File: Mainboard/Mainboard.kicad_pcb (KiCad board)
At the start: 2 copper layers, 46 parts, among them IC1 REF102AU_2K5, IC4 DAC8814IBDBT, J1 5745782-6, J2 5745782-6, J3 5745782-6, U1 Teensy4.0, U11 ADG419BR, U12 ADG419BR, U7 ADG419BR, U8 LTC2326CMS-16-PBF, U9 LT1469CS8-TRPBF

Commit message: working mainboard push!
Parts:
- removed C121: 330u 25V, Capacitor_THT:CP_Radial_D8.0mm_P3.50mm
- removed C126, C127, C128, C129, C133, C135, C136, C137: 10u, Capacitor_SMD:C_1206_3216Metric
- removed TP1, TP2, TP3, TP4, TP5, TP6, TP7, TP8: TestPoint, TestPoint:TestPoint_Loop_D1.80mm_Drill1.0mm_Beaded
- added A1: Pololu_Breakout_A4988, Module:Pololu_Breakout-16_15.2x20.3mm, F.Cu at (179.3, 120.8)
- added A2: Pololu_Breakout_A4988, Module:Pololu_Breakout-16_15.2x20.3mm, F.Cu at (158.6, 111.1)
- added A3: Pololu_Breakout_A4988, Module:Pololu_Breakout-16_15.2x20.3mm, F.Cu at (158.6, 133.9)
- added C10: 4.7n, Capacitor_SMD:C_0805_2012Metric, F.Cu at (138.6, 95.2)
- added C11: 4.7n, Capacitor_SMD:C_0805_2012Metric, F.Cu at (140.1, 82.8)
- added C12: 4.7n, Capacitor_SMD:C_0805_2012Metric, F.Cu at (144.6, 87.8)
- added C13: 4.7n, Capacitor_SMD:C_0805_2012Metric, F.Cu at (144.6, 63.2)
- added C14: 4.7n, Capacitor_SMD:C_0805_2012Metric, F.Cu at (138.6, 70.8)
- added C15: 4.7n, Capacitor_SMD:C_0805_2012Metric, F.Cu at (140.1, 58.8)
- added C16: 3.3n, Capacitor_SMD:C_0805_2012Metric, F.Cu at (164.5, 78.4)
- added C17: 100n, Capacitor_SMD:C_0805_2012Metric, F.Cu at (135.1, 63.8)
- added C18: 100n, Capacitor_SMD:C_0805_2012Metric, F.Cu at (145.1, 67.8)
- added C19: 100n, Capacitor_SMD:C_0805_2012Metric, F.Cu at (145.1, 92.2)
- added C20: 100n, Capacitor_SMD:C_0805_2012Metric, F.Cu at (135.1, 86.3)
- added C21: 3.3n, Capacitor_SMD:C_0805_2012Metric, F.Cu at (179.0, 70.3)
- added C22: 3.3n, Capacitor_SMD:C_0805_2012Metric, F.Cu at (179.0, 78.3)
- added C23: 3.3n, Capacitor_SMD:C_0805_2012Metric, F.Cu at (164.5, 70.4)
- added C24: 4.7n, Capacitor_SMD:C_0805_2012Metric, F.Cu at (157.2, 80.3)
- added C25: 4.7n, Capacitor_SMD:C_0805_2012Metric, F.Cu at (171.6, 67.3)
- added C26: 4.7n, Capacitor_SMD:C_0805_2012Metric, F.Cu at (171.6, 80.3)
- added C27: 4.7n, Capacitor_SMD:C_0805_2012Metric, F.Cu at (157.2, 67.3)
- added C28: 100n, Capacitor_SMD:C_0805_2012Metric, F.Cu at (175.6, 119.8)
- added C29: 3.3n, Capacitor_SMD:C_0805_2012Metric, F.Cu at (173.4, 94.4)
- added C30: 3.3n, Capacitor_SMD:C_0805_2012Metric, F.Cu at (180.2, 103.5)
- added C31: 3.3n, Capacitor_SMD:C_0805_2012Metric, F.Cu at (173.6, 104.7)
- added C32: 3.3n, Capacitor_SMD:C_0805_2012Metric, F.Cu at (185.3, 103.5)
- added C33: 47u, Capacitor_SMD:C_0805_2012Metric, F.Cu at (192.3, 93.7)
- added C34: 100n, Capacitor_SMD:C_0805_2012Metric, F.Cu at (188.6, 93.7)
- added C35: 10u, Capacitor_THT:CP_Radial_D5.0mm_P2.00mm, F.Cu at (181.6, 88.9)
- added C36: 100n, Capacitor_SMD:C_0805_2012Metric, F.Cu at (182.6, 93.2)
- added C37: 100n, Capacitor_SMD:C_0805_2012Metric, F.Cu at (175.6, 142.8)
- added C38: 100n, Capacitor_SMD:C_0805_2012Metric, F.Cu at (196.3, 129.6)
- added C39: 100n, Capacitor_SMD:C_0805_2012Metric, F.Cu at (209.7, 78.1)
- added C40: 100n, Capacitor_SMD:C_0805_2012Metric, F.Cu at (167.9, 74.4)
- added C41: 100n, Capacitor_SMD:C_0805_2012Metric, F.Cu at (179.0, 74.3)
- added C42: 100n, Capacitor_SMD:C_0805_2012Metric, F.Cu at (153.4, 74.4)
- added C43: 100n, Capacitor_SMD:C_0805_2012Metric, F.Cu at (164.5, 74.4)
- added C44: 100n, Capacitor_SMD:C_0805_2012Metric, F.Cu at (195.6, 60.8)
- added C45: 100n, Capacitor_SMD:C_0805_2012Metric, F.Cu at (192.1, 50.0)
- added C46: 100n, Capacitor_SMD:C_0805_2012Metric, F.Cu at (164.5, 58.0)
- added C47: 100n, Capacitor_SMD:C_0805_2012Metric, F.Cu at (153.8, 61.2)
- added C79: 100u, Capacitor_THT:CP_Radial_D6.3mm_P2.50mm, F.Cu at (152.6, 128.9)
- added C8: 2.2u, Capacitor_SMD:C_0805_2012Metric, F.Cu at (187.4, 50.0)
- added C80: 100u, Capacitor_THT:CP_Radial_D6.3mm_P2.50mm, F.Cu at (184.6, 144.4)
- added C83: 100u, Capacitor_THT:CP_Radial_D6.3mm_P2.50mm, F.Cu at (152.6, 151.8)
- added C84: 10u, Capacitor_THT:CP_Radial_D5.0mm_P2.00mm, F.Cu at (182.1, 56.8)
- added C85: 100u, Capacitor_THT:CP_Radial_D6.3mm_P2.50mm, F.Cu at (182.1, 47.9)
- added H1: MountingHole_Pad, MountingHole:MountingHole_2.2mm_M2_Pad_Via, F.Cu at (220.3, 154.8)
- added J4: Conn_01x02_Pin, Connector_PinHeader_2.54mm:PinHeader_1x02_P2.54mm_Vertical, F.Cu at (158.3, 88.1)
- added J5: Conn_01x02_Pin, Connector_PinHeader_2.54mm:PinHeader_1x02_P2.54mm_Vertical, F.Cu at (189.8, 100.3)
- added R19: 1k, Resistor_SMD:R_0805_2012Metric, F.Cu at (191.1, 47.5)
- added R20: 3k, Resistor_SMD:R_0805_2012Metric, F.Cu at (138.6, 98.8)
- added R21: 220, Resistor_SMD:R_0805_2012Metric, F.Cu at (135.1, 94.2)
- added R22: 3k, Resistor_SMD:R_0805_2012Metric, F.Cu at (145.2, 95.3)
- added R23: 3k, Resistor_SMD:R_0805_2012Metric, F.Cu at (145.2, 98.7)
- added R24: 220, Resistor_SMD:R_0805_2012Metric, F.Cu at (135.1, 81.8)
- added R25: 3k, Resistor_SMD:R_0805_2012Metric, F.Cu at (140.1, 79.2)
- added R26: 3k, Resistor_SMD:R_0805_2012Metric, F.Cu at (146.8, 84.1)
- added R27: 3k, Resistor_SMD:R_0805_2012Metric, F.Cu at (148.1, 87.8)
- added R28: 3k, Resistor_SMD:R_0805_2012Metric, F.Cu at (145.0, 79.2)
- added R29: 3k, Resistor_SMD:R_0805_2012Metric, F.Cu at (145.0, 74.3)
- added R30: 1M2, Resistor_SMD:R_0805_2012Metric, F.Cu at (209.8, 81.9)
- added R31: 3k, Resistor_SMD:R_0805_2012Metric, F.Cu at (145.1, 70.8)
- added R32: 3k, Resistor_SMD:R_0805_2012Metric, F.Cu at (144.6, 55.8)
- added R33: 3k, Resistor_SMD:R_0805_2012Metric, F.Cu at (146.6, 59.8)
- added R34: 3k, Resistor_SMD:R_0805_2012Metric, F.Cu at (147.6, 63.2)
- added R35: 3k, Resistor_SMD:R_0805_2012Metric, F.Cu at (138.6, 74.2)
- added R36: 3k, Resistor_SMD:R_0805_2012Metric, F.Cu at (140.1, 55.8)
- added R37: 220, Resistor_SMD:R_0805_2012Metric, F.Cu at (135.1, 73.2)
- added R38: 220, Resistor_SMD:R_0805_2012Metric, F.Cu at (135.1, 59.3)
- added R39: 10k, Resistor_SMD:R_0805_2012Metric, F.Cu at (188.5, 67.8)
- added R40: 1.5k, Resistor_SMD:R_0805_2012Metric, F.Cu at (161.2, 64.4)
- added R41: 1.5k, Resistor_SMD:R_0805_2012Metric, F.Cu at (175.6, 80.3)
- added R42: 1.5k, Resistor_SMD:R_0805_2012Metric, F.Cu at (175.5, 64.3)
- added R43: 1.5k, Resistor_SMD:R_0805_2012Metric, F.Cu at (161.2, 80.3)
- added R50: 3k, Resistor_SMD:R_0805_2012Metric, F.Cu at (161.2, 83.1)
- added R51: 3k, Resistor_SMD:R_0805_2012Metric, F.Cu at (157.2, 83.1)
- added R52: 3k, Resistor_SMD:R_0805_2012Metric, F.Cu at (175.5, 67.3)
- added R53: 3k, Resistor_SMD:R_0805_2012Metric, F.Cu at (171.5, 64.3)
- added R54: 3k, Resistor_SMD:R_0805_2012Metric, F.Cu at (175.5, 83.3)
- added R55: 3k, Resistor_SMD:R_0805_2012Metric, F.Cu at (171.5, 83.3)
- added R56: 3k, Resistor_SMD:R_0805_2012Metric, F.Cu at (161.2, 67.3)
- added R57: 3k, Resistor_SMD:R_0805_2012Metric, F.Cu at (157.2, 64.4)
- added R58: 3k, Resistor_SMD:R_0805_2012Metric, F.Cu at (164.5, 62.2)
- added R59: 470, Resistor_SMD:R_0805_2012Metric, F.Cu at (164.5, 88.8)
- added R60: 100, Resistor_SMD:R_0805_2012Metric, F.Cu at (195.9, 88.2)
- added R61: 470, Resistor_SMD:R_0805_2012Metric, F.Cu at (169.3, 94.4)
- added R62: 470, Resistor_SMD:R_0805_2012Metric, F.Cu at (164.5, 99.0)
- added R63: 470, Resistor_SMD:R_0805_2012Metric, F.Cu at (169.3, 104.7)
- added R64: 10k, Resistor_SMD:R_0805_2012Metric, F.Cu at (195.9, 90.4)
- added U10: TL072, Package_SO:SOIC-8-1EP_3.9x4.9mm_P1.27mm_EP2.29x3mm_ThermalVias, F.Cu at (157.0, 93.4)
- added U2: TL072, Package_SO:SOIC-8-1EP_3.9x4.9mm_P1.27mm_EP2.29x3mm_ThermalVias, F.Cu at (194.6, 55.5)
- added U3: TL072, Package_SO:SOIC-8-1EP_3.9x4.9mm_P1.27mm_EP2.29x3mm_ThermalVias, F.Cu at (139.6, 89.4)
- added U4: TL072, Package_SO:SOIC-8-1EP_3.9x4.9mm_P1.27mm_EP2.29x3mm_ThermalVias, F.Cu at (139.6, 65.1)
- added U5: TL074, Package_SO:SOIC-14_3.9x8.7mm_P1.27mm, F.Cu at (159.0, 73.8)
- added U6: TL074, Package_SO:SOIC-14_3.9x8.7mm_P1.27mm, F.Cu at (173.5, 73.7)
- C122, C123, C124, C125, C130, C131, C132, C134: value 10u -> 100n; footprint Capacitor_SMD:C_1206_3216Metric -> Capacitor_SMD:C_0805_2012Metric
- C77, C78, C81, C82: value 330u 25V -> 10u; footprint Capacitor_THT:CP_Radial_D8.0mm_P3.50mm -> Capacitor_THT:CP_Radial_D5.0mm_P2.00mm
- moved JP12 102.8 mm to (214.3, 81.9), turned to 180 degrees
- moved JP29 100.7 mm to (214.2, 78.1), turned to 180 degrees
- moved J1 89.0 mm to (214.2, 45.5), turned to 90 degrees
- moved JP32 76.1 mm to (194.1, 97.5)
- moved JP33 75.9 mm to (194.1, 100.7)
- moved U1 74.0 mm to (138.2, 43.9)
- moved IC1 71.5 mm to (188.4, 55.5), turned to 90 degrees
- moved U12 70.8 mm to (174.1, 100.2)
- moved JP31 69.9 mm to (168.0, 99.0), turned to 90 degrees
- moved C82 67.7 mm to (204.0, 62.5), turned to -90 degrees
- moved U11 67.6 mm to (174.1, 90.0)
- moved C81 66.6 mm to (204.0, 55.5), turned to -90 degrees
- moved U8 66.0 mm to (189.4, 89.9)
- moved C78 65.5 mm to (204.0, 48.5), turned to -90 degrees
- moved C77 64.0 mm to (204.0, 43.5), turned to 90 degrees
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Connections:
- net /ADC/AIN+ renamed /AIN+
- net /ADC/AIN- renamed /AIN-
- net /DAC/BIAS_MOD renamed /BIAS_MOD
- net /DAC/CS_DAC renamed /CS_DAC
- net /DAC/MOSI_DAC renamed /MOSI_DAC
- C130 pad 1: -15V -> +3V3
- C131 pad 2: +15V -> +5V
- C132 pad 1: -15V -> GND
- C132 pad 2: GND -> +5V
- C134 pad 1: -15V -> +3V3
- IC4 pad 21: /DAC/LDAC_DAC -> /LDAC_DAC
- IC4 pad 9: /DAC/SCK_DAC -> /SCK_ADC
- J1 pad MH1: /Shield -> Shield
- J1 pad MH2: /Shield -> Shield
- J2 pad 1: /Connectors/T_Amp+ -> /T_Amp-
- J2 pad 14: GND -> unconnected-(J2-Pad14)
- J2 pad 15: GND -> /Z-Y
- J2 pad 2: /Connectors/T_Amp- -> /T_Amp+
- J2 pad 3: unconnected-(J2-Pad3) -> GND
- J2 pad 4: unconnected-(J2-Pad4) -> /Z+X
- J2 pad 5: unconnected-(J2-Pad5) -> /Z-X
- J2 pad 7: unconnected-(J2-Pad7) -> /Connectors/BIAS
- J2 pad 8: unconnected-(J2-Pad8) -> /Z+Y
- J2 pad MH1: GND -> Shield
- J2 pad MH2: GND -> Shield
- J3 pad 1: unconnected-(J3-Pad1) -> /2B_3
- J3 pad 10: unconnected-(J3-Pad10) -> -15V
- J3 pad 11: unconnected-(J3-Pad11) -> GND
- J3 pad 12: unconnected-(J3-Pad12) -> /2B_2
- J3 pad 13: unconnected-(J3-Pad13) -> /1A_2
- J3 pad 14: unconnected-(J3-Pad14) -> /2B_1
- J3 pad 15: unconnected-(J3-Pad15) -> /1B_1
- J3 pad 2: unconnected-(J3-Pad2) -> /2A_3
- J3 pad 3: unconnected-(J3-Pad3) -> /1A_3
- J3 pad 4: unconnected-(J3-Pad4) -> /1B_3
- J3 pad 5: unconnected-(J3-Pad5) -> /2A_2
- J3 pad 6: unconnected-(J3-Pad6) -> /1B_2
- J3 pad 7: unconnected-(J3-Pad7) -> /2A_1
- J3 pad 8: unconnected-(J3-Pad8) -> /1A_1
- J3 pad 9: unconnected-(J3-Pad9) -> +15V
- J3 pad MH1: GND -> Shield
- J3 pad MH2: GND -> Shield
- JP12 pad 1: /Shield -> Shield
- JP29 pad 1: /Shield -> Shield
- JP30 pad 1: /ADC/T_Amp+ -> /T_Amp+
- JP31 pad 1: /ADC/T_Amp- -> /T_Amp-
- U1 pad 11: /DAC/LDAC_DAC -> /CS_ADC
- U1 pad 14: unconnected-(U1-12_MISO_MQSL-Pad14) -> /MISO_ADC
- U1 pad 17: GND -> unconnected-(U1-GND-Pad17)
- U1 pad 2: unconnected-(U1-0_RX1_CRX2_CS1-Pad2) -> /BIAS_MOD_EN
- U1 pad 20: /DAC/SCK_DAC -> /SCK_ADC
- U1 pad 21: unconnected-(U1-14_A0_TX3_SPDIF_OUT-Pad21) -> /StepperDrivers/DIR_1
- U1 pad 22: unconnected-(U1-15_A1_RX3_SPDIF_IN-Pad22) -> /StepperDrivers/STEP_1
- U1 pad 3: unconnected-(U1-1_TX1_CTX2_MISO1-Pad3) -> /StepperDrivers/STEP_3
- U1 pad 32: GND -> unconnected-(U1-GND-Pad32)
- U1 pad 4: unconnected-(U1-2_OUT2-Pad4) -> /StepperDrivers/DIR_3
- U1 pad 5: unconnected-(U1-3_LRCLK2-Pad5) -> /StepperDrivers/STEP_2
- U1 pad 6: unconnected-(U1-4_BCLK2-Pad6) -> /StepperDrivers/DIR_2
- U1 pad 7: unconnected-(U1-5_IN2-Pad7) -> /BUSY_ADC
- U1 pad 8: unconnected-(U1-6_OUT1D-Pad8) -> /CNV_ADC
- U1 pad 9: unconnected-(U1-7_RX2_OUT1A-Pad9) -> /LDAC_DAC
- U11 pad 2: /ADC/T_Amp+ -> /T_Amp+
- U12 pad 2: /ADC/T_Amp- -> /T_Amp-
- U7 pad 6: /DAC/BIAS_MOD_EN -> /BIAS_MOD_EN
- U8 pad 11: /ADC/BUSY_ADC -> /BUSY_ADC
- U8 pad 12: /ADC/~CS_ADC -> /CS_ADC
- U8 pad 13: /ADC/SCK_ADC -> /SCK_ADC
- U8 pad 9: /ADC/CNV -> /CNV_ADC
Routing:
- net +5V: track 0.00 -> 215.9 mm, vias 0 -> 6
- net GND: track 0.00 -> 161.3 mm, vias 0 -> 56
- net /StepperDrivers/STEP_1: track 0.00 -> 135.6 mm, vias 0 -> 3
- net /StepperDrivers/DIR_1: track 0.00 -> 130.1 mm, vias 0 -> 2
- net /StepperDrivers/STEP_3: track 0.00 -> 120.6 mm, vias 0 -> 2
- net /StepperDrivers/DIR_3: track 0.00 -> 119.3 mm, vias 0 -> 3
- net /StepperDrivers/STEP_2: track 0.00 -> 107.7 mm
- net /PS_Temp_SCL: track 0.00 -> 107.0 mm, vias 0 -> 2
- net /StepperDrivers/DIR_2: track 0.00 -> 105.6 mm
- net -15V: track 0.00 -> 102.2 mm, vias 0 -> 10
- net +15V: track 0.00 -> 101.2 mm, vias 0 -> 10
- net /PS_Temp_SDA: track 0.00 -> 92.5 mm
- net /CNV_ADC: track 0.00 -> 85.8 mm, vias 0 -> 3
- net +3V3: track 0.00 -> 84.9 mm, vias 0 -> 4
- net /BUSY_ADC: track 0.00 -> 84.8 mm, vias 0 -> 2
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- added copper zone on In1.Cu, net +15V
- added copper zone on In1.Cu, net +3V3
- added copper zone on In2.Cu, net +5V
- added copper zone on In2.Cu, net -15V
- added copper zone on B.Cu, net GND
- added copper zone on F.Cu, net Shield
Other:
- board outline added: 106.1 x 132 mm
- copper layers 2 -> 4

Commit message: more push
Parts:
- added G***: LOGO, LOGO, F.Cu at (210.0, 126.8)
- added G***: LOGO, LOGO, F.Cu at (189.6, 110.9)
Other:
- board text added: "STM Mainboard Author: Gautham Anne 4/02/2025"
- board text added: "V1.1"

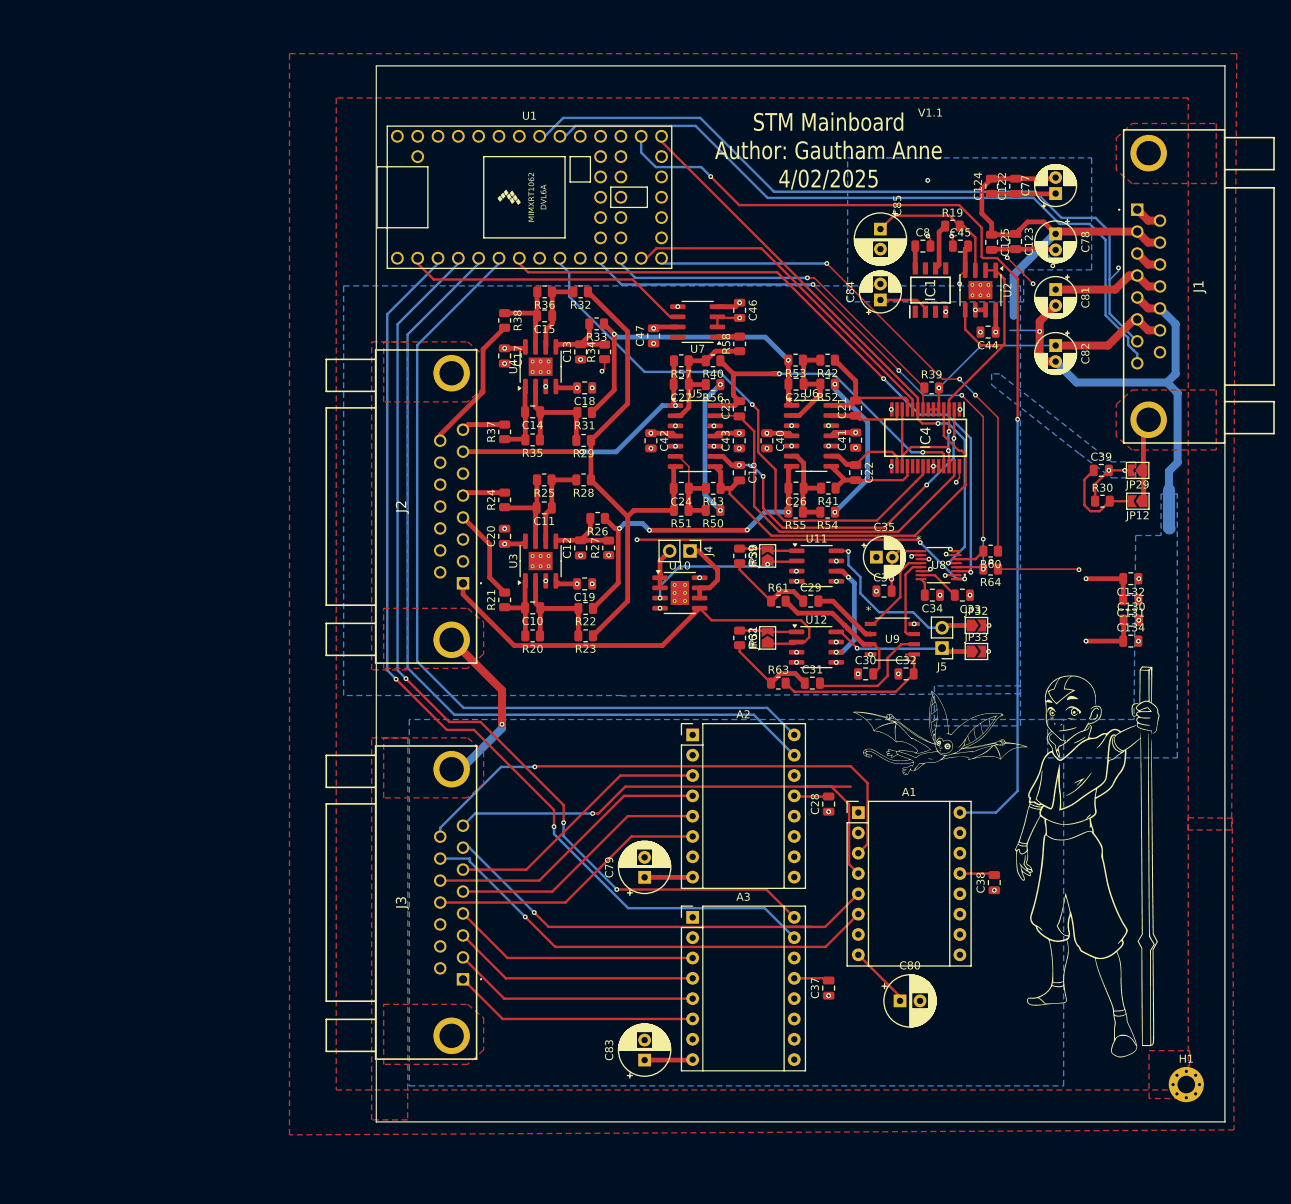
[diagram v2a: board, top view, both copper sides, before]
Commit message: mainboard working commits!
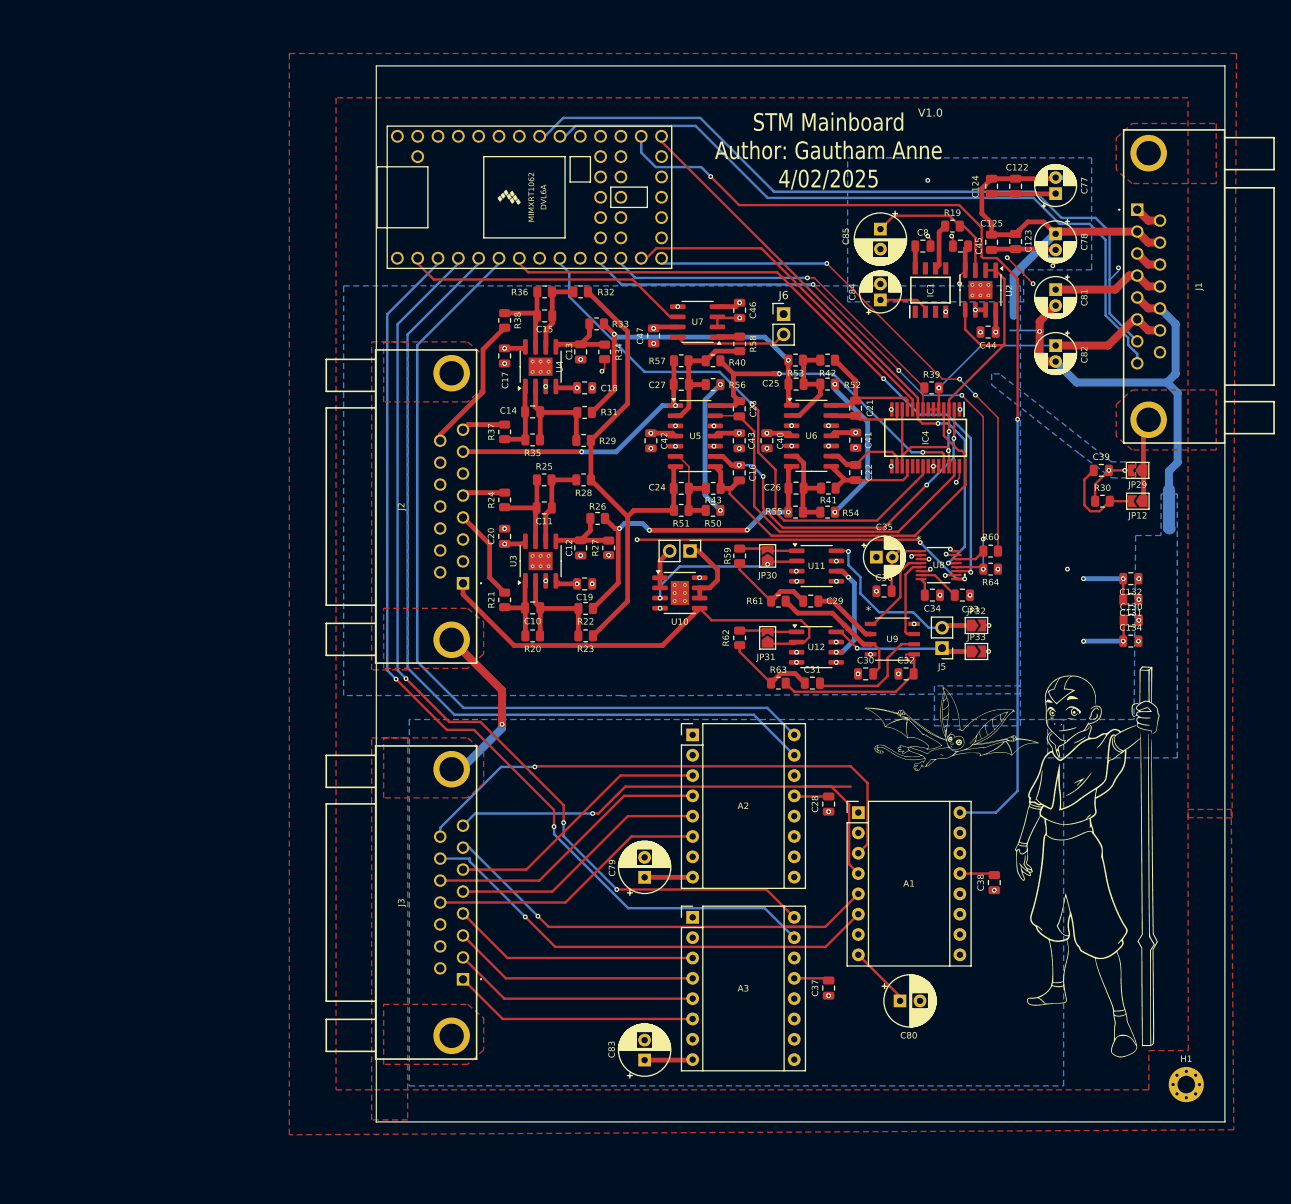
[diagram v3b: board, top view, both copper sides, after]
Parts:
- added J6: Conn_01x02_Pin, Connector_PinHeader_2.54mm:PinHeader_1x02_P2.54mm_Vertical, F.Cu at (170.0, 58.5)
- moved G*** 1.51 mm to (191.0, 110.4)
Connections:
- J2 pad 14: unconnected-(J2-Pad14) -> GND
- J2 pad 6: unconnected-(J2-Pad6) -> GND
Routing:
- net /BIAS_MOD: track 0.00 -> 14.0 mm
- net GND: track 161.3 -> 163.2 mm
- net +3V3: track 84.9 -> 83.8 mm, vias 4 -> 5
- net +5V: track 215.9 -> 215.4 mm, vias 6 -> 7
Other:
- board text added: "Analog"
- board text added: "Digital"
- board text added: "V1.0"
- board text removed: "V1.1"

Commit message: final assembly updates!
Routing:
- net GND: track 163.2 -> 159.4 mm, vias 56 -> 55
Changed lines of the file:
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@@
-	)
-	(via
-		(at 202 60.697)
-		(size 0.6)
-		(drill 0.3)
-		(layers "F.Cu" "B.Cu")
-		(net 1)
 	)
 	(via
@@
 	)
 	(segment
-		(start 201.8665 60.5635)
-		(end 202 60.697)
-		(width 0.2)
-		(layer "B.Cu")
-		(net 1)
-	)
-	(segment
 		(start 217.05 57.813)
 		(end 219 59.763)
@@
 		(layer "B.Cu")
 		(net 1)
-	)
-	(segment
-		(start 198.305 60.5635)
-		(end 201.8665 60.5635)
-		(width 0.2)
-		(layer "B.Cu")
-		(net 1)

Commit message: cad update
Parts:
- moved A3 28.3 mm to (130.7, 129.3)
- moved C134 28.3 mm to (185.4, 94.7)
- moved C24 28.3 mm to (129.3, 75.6)
- moved C25 28.3 mm to (143.6, 62.6)
- moved C26 28.3 mm to (143.6, 75.6)
- moved C27 28.3 mm to (129.3, 62.6)
- moved C37 28.3 mm to (147.7, 138.1)
- moved C38 28.3 mm to (168.4, 124.9)
- moved C80 28.3 mm to (156.6, 139.7)
- moved J1 28.3 mm to (186.3, 40.8)
- moved J4 28.3 mm to (130.3, 83.5)
- moved J5 28.3 mm to (161.8, 95.6)
- moved R40 28.3 mm to (133.2, 59.7)
- moved R41 28.3 mm to (147.6, 75.6)
- moved R43 28.3 mm to (133.3, 75.6)
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
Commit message: updates!
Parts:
- moved H1 154.6 mm to (85.1, 38.8), turned to 180 degrees
- moved J1 143.4 mm to (91.2, 148.2), turned to -90 degrees
- moved C77 134.1 mm to (101.4, 150.2), turned to -90 degrees
- moved C122 130.4 mm to (106.4, 151.1), turned to -90 degrees
- moved C124 127.5 mm to (109.4, 151.1), turned to -90 degrees
- moved C78 125.8 mm to (101.4, 145.2), turned to 90 degrees
- moved U1 124.3 mm to (167.2, 149.8), turned to 180 degrees
- moved C123 118.6 mm to (106.4, 144.2), turned to 90 degrees
- moved C125 115.3 mm to (109.4, 144.1), turned to 90 degrees
- moved C81 114.9 mm to (101.4, 138.2), turned to 90 degrees
- moved R19 114.2 mm to (114.3, 146.1), turned to 180 degrees
- moved J3 112.4 mm to (175.5, 52.0), turned to 90 degrees
- moved C45 110.7 mm to (113.3, 143.6), turned to 180 degrees
- moved C83 108.9 mm to (152.8, 41.9), turned to -90 degrees
- moved C85 107.1 mm to (123.3, 145.8), turned to 90 degrees
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
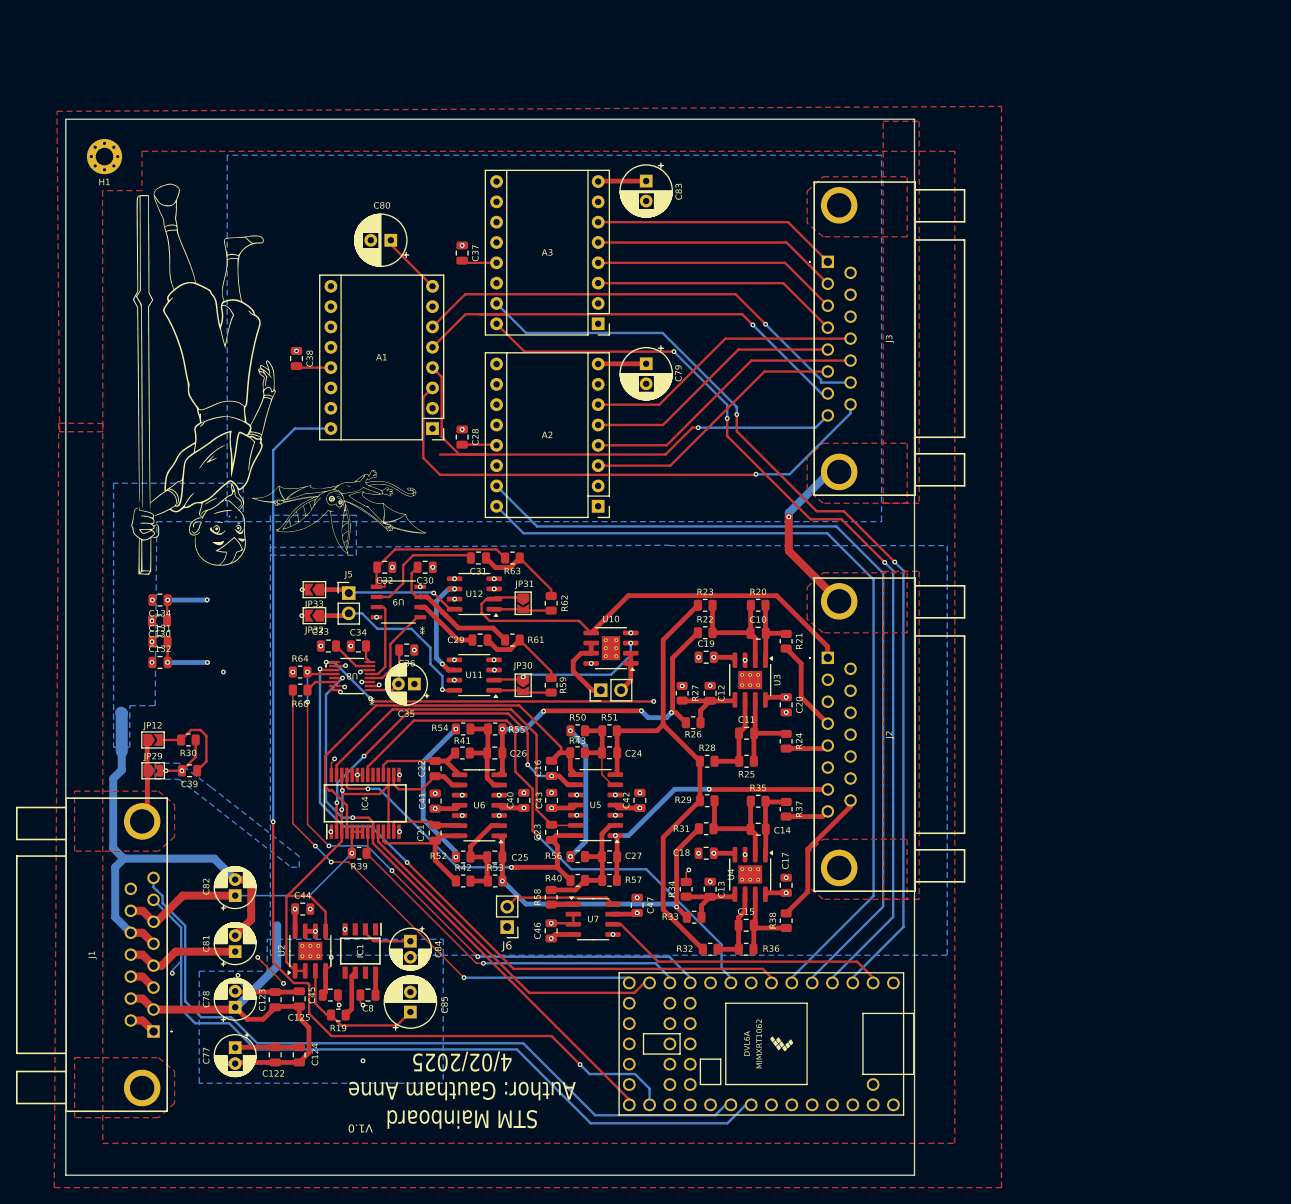
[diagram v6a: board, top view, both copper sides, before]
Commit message: updates to DAC + ADC Libraries
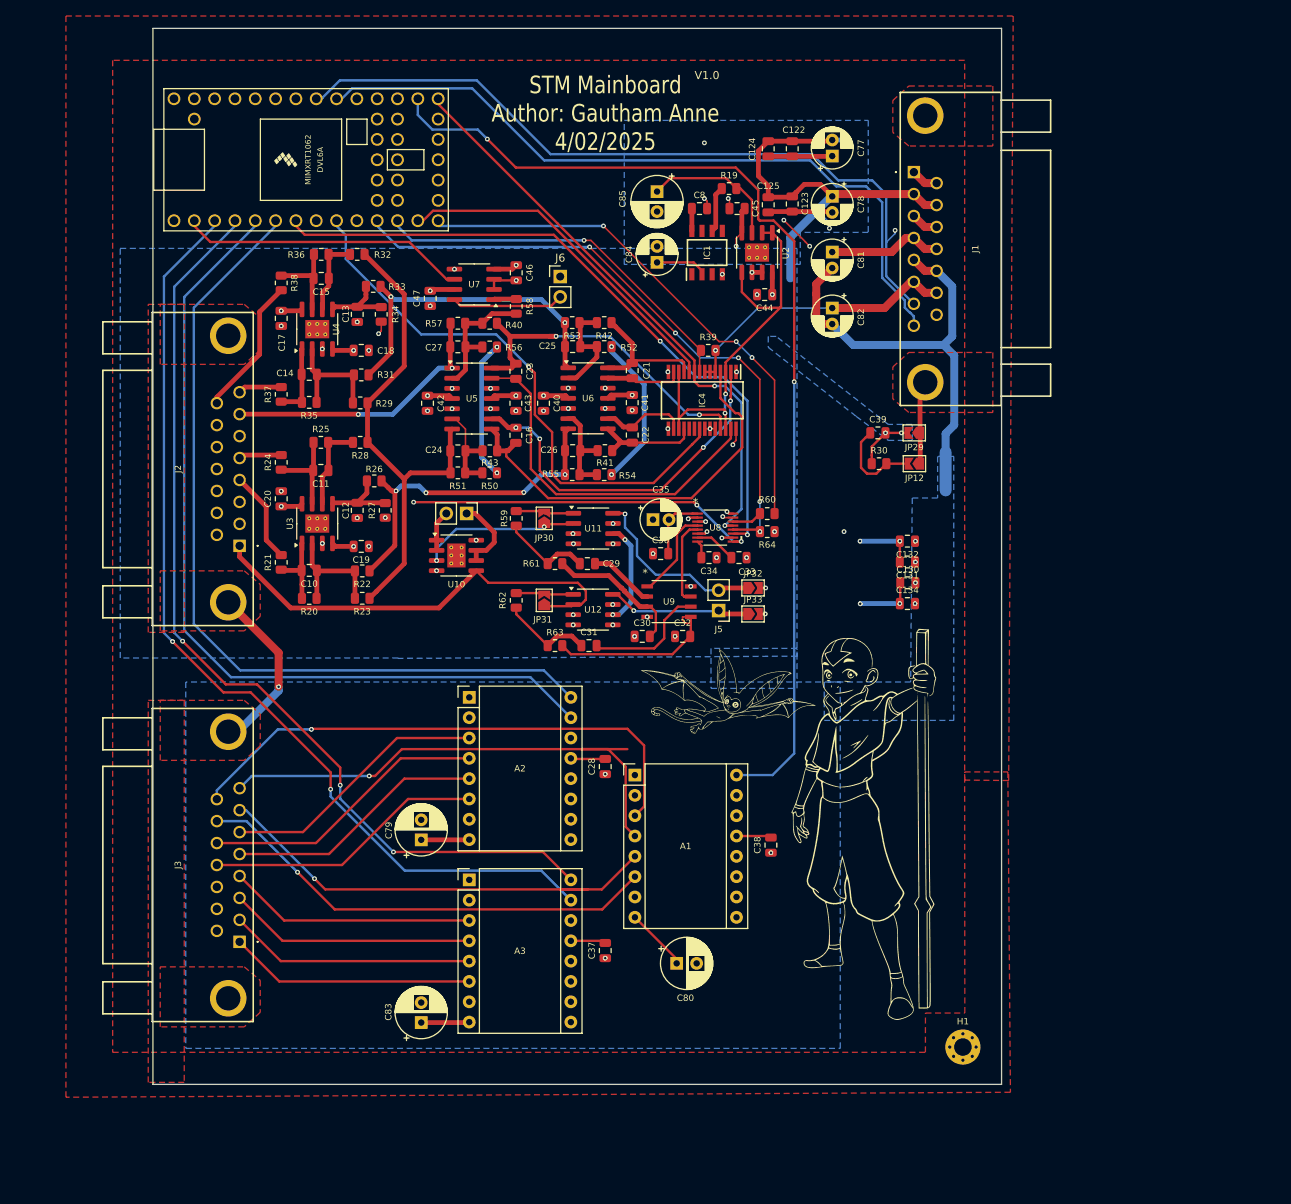
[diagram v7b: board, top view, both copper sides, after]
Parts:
- moved H1 154.6 mm to (192.4, 150.1), turned to 0 degrees
- moved J1 143.4 mm to (186.3, 40.8), turned to 90 degrees
- moved C77 134.1 mm to (176.1, 38.8), turned to 90 degrees
- moved C122 130.4 mm to (171.1, 37.9), turned to 90 degrees
- moved C124 127.5 mm to (168.1, 37.9), turned to 90 degrees
- moved C78 125.9 mm to (176.1, 43.8), turned to -90 degrees
- moved U1 124.3 mm to (110.3, 39.2), turned to 0 degrees
- moved C123 118.6 mm to (171.1, 44.8), turned to -90 degrees
- moved C125 115.3 mm to (168.1, 44.9), turned to -90 degrees
- moved C81 115.0 mm to (176.1, 50.8), turned to -90 degrees
- moved R19 114.3 mm to (163.2, 42.8), turned to 0 degrees
- moved J3 112.4 mm to (102.0, 137.0), turned to -90 degrees
- moved C45 110.7 mm to (164.2, 45.3), turned to 0 degrees
- moved C83 108.9 mm to (124.7, 147.1), turned to 90 degrees
- moved C85 107.1 mm to (154.2, 43.2), turned to -90 degrees
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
